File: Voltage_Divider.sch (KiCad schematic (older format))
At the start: 53 parts, among them J24 test, J25 CONN_01X05, J26 test, J27 test, J28 test, J29 test, U19 AQV258, U20 AQV258, U21 ANA4522, U22 ANA4522

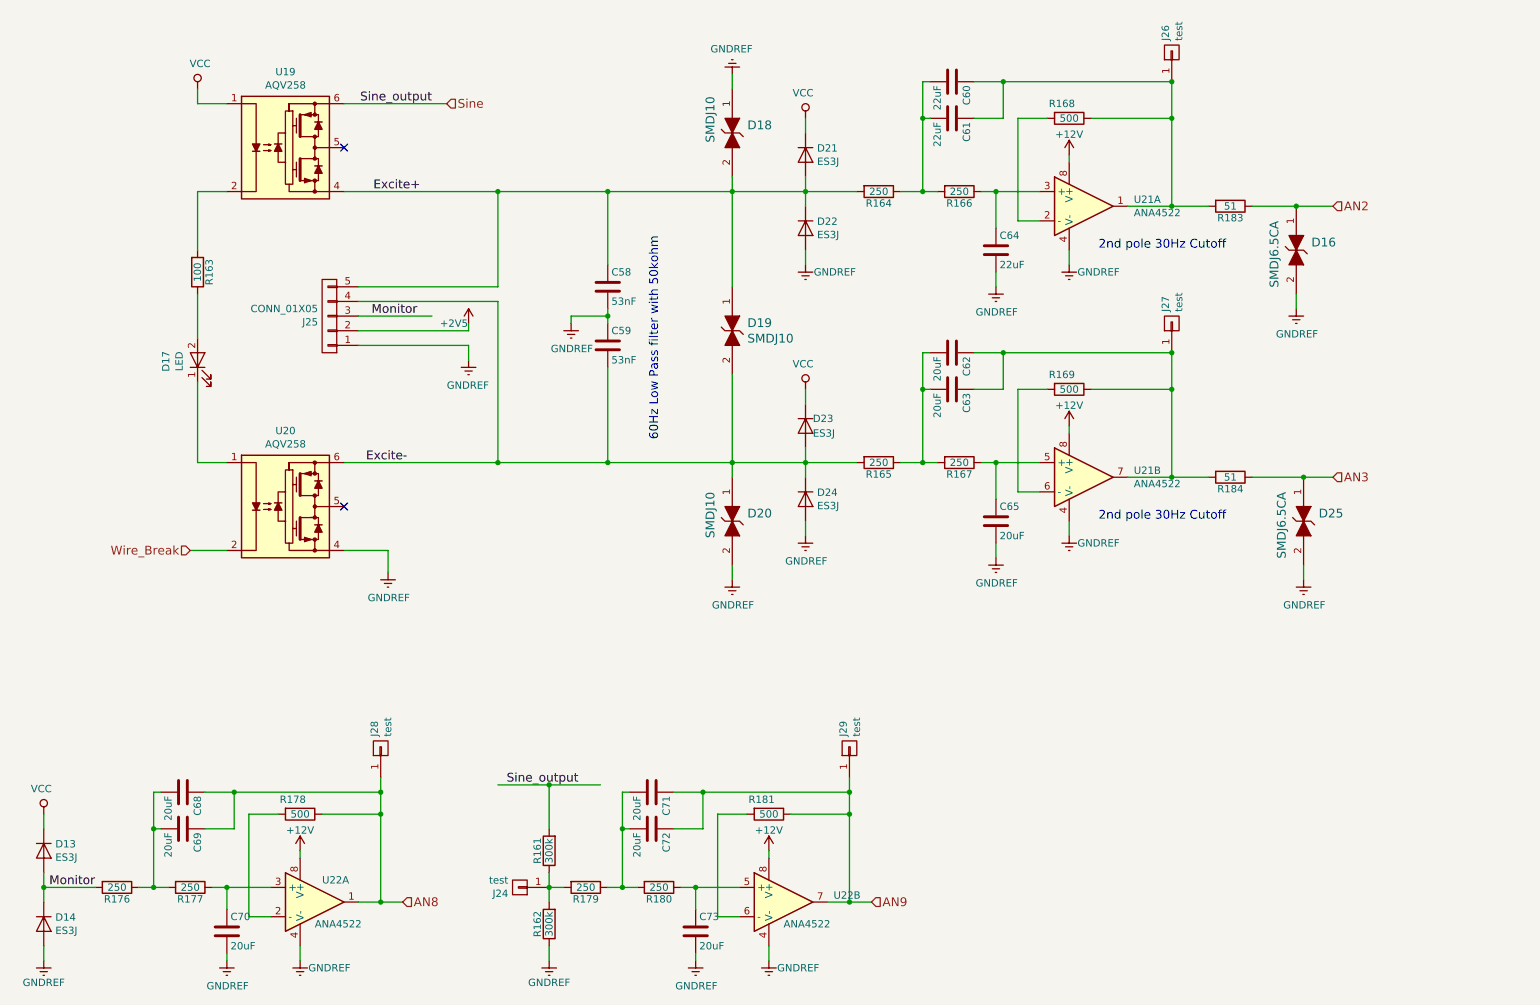
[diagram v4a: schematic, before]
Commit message: 4차 PCB
U23 Wire Breakage Relay 추가
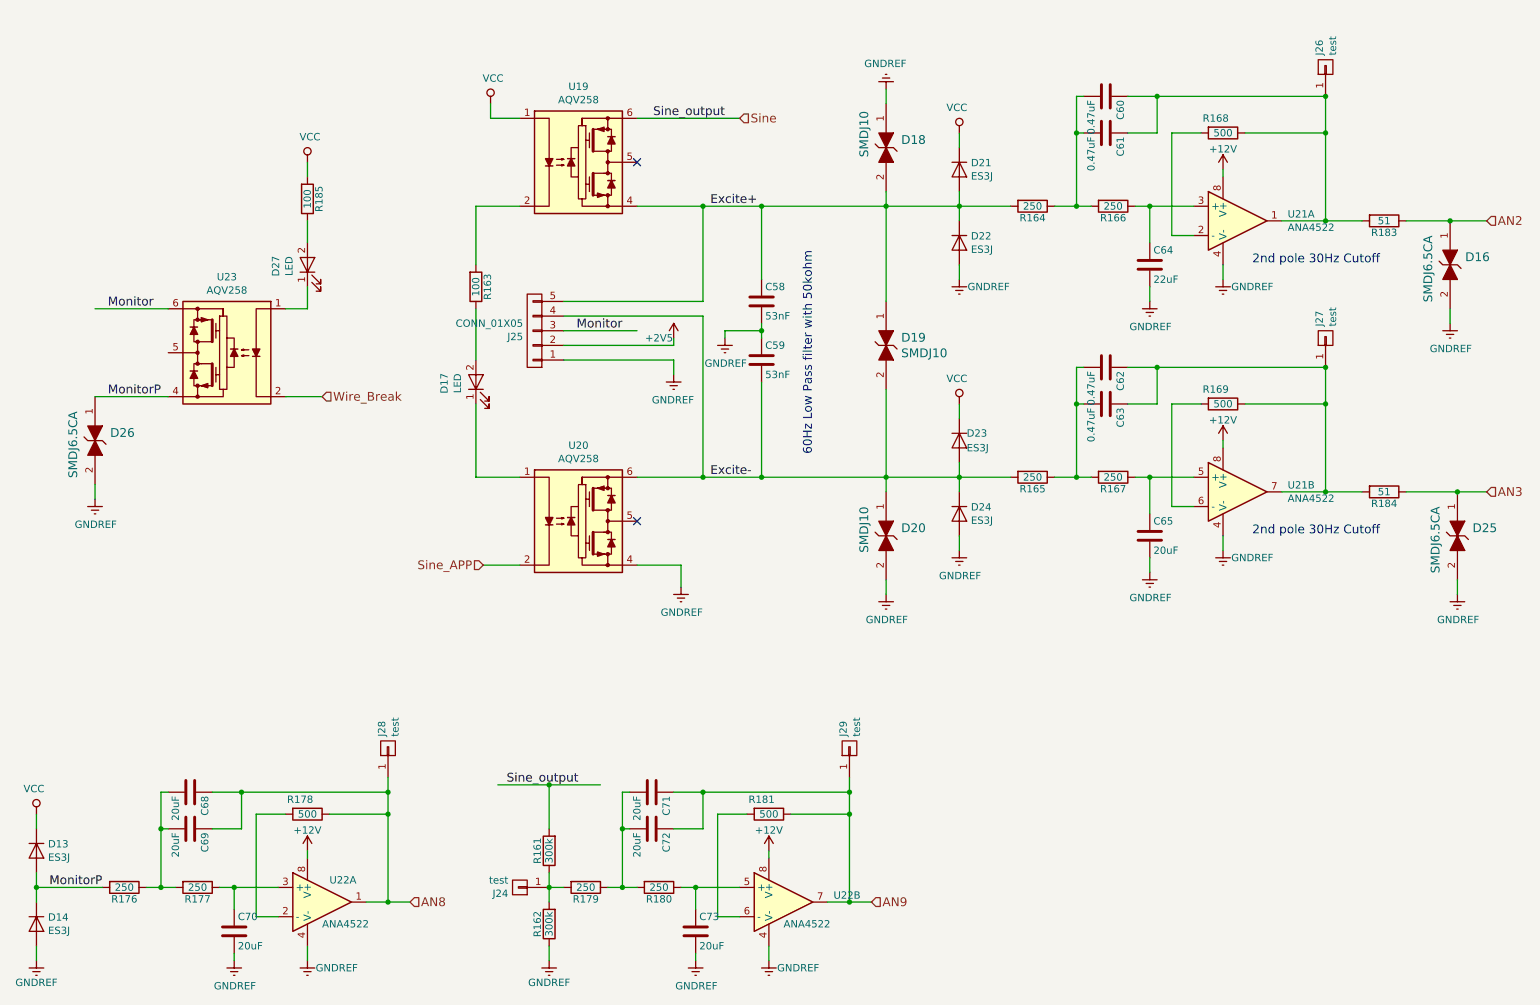
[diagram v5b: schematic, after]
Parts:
- added D26: SMDJ6.5CA, Diodes_SMD:D_SMC_Handsoldering, symbol PGB1010603MR
- added D27: LED, LEDs:LED_D5.0mm, symbol LED
- added R185: 100, Resistors_SMD:R_0805_HandSoldering, symbol R
- added U23: AQV258, Housings_DIP:DIP-6_W7.62mm_Socket, symbol AQV258
- C60, C61: value 22uF -> 0.47uF
- C62, C63: value 20uF -> 0.47uF
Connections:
- net GNDREF: now also D26.2
- net Monitor: now also U23.6 (VCC); no longer D13.2 (A), D14.1 (K), R176.2
- net VCC: now also R185.2
- net Wire_Break: now also U23.2 (C); no longer U20.2 (C)
- new net: D27.1 (K), U23.1 (A)
- new net: D27.2 (A), R185.1
- new net MonitorP: D13.2 (A), D14.1 (K), D26.1, R176.2, U23.4 (VEE)
- new net Sine_APP: U20.2 (C)
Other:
- moved on the sheet: C58, C59, C60, C61, C62, C63, C64, C65, C68, C69, C70, D13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
